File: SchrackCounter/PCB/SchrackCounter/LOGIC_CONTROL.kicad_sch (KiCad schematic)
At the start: 7 parts, among them U2 LDD080BUE-101A, U3 LTD080BUE-103A, U4 LDD080BUE-101A, U5 MAX7219

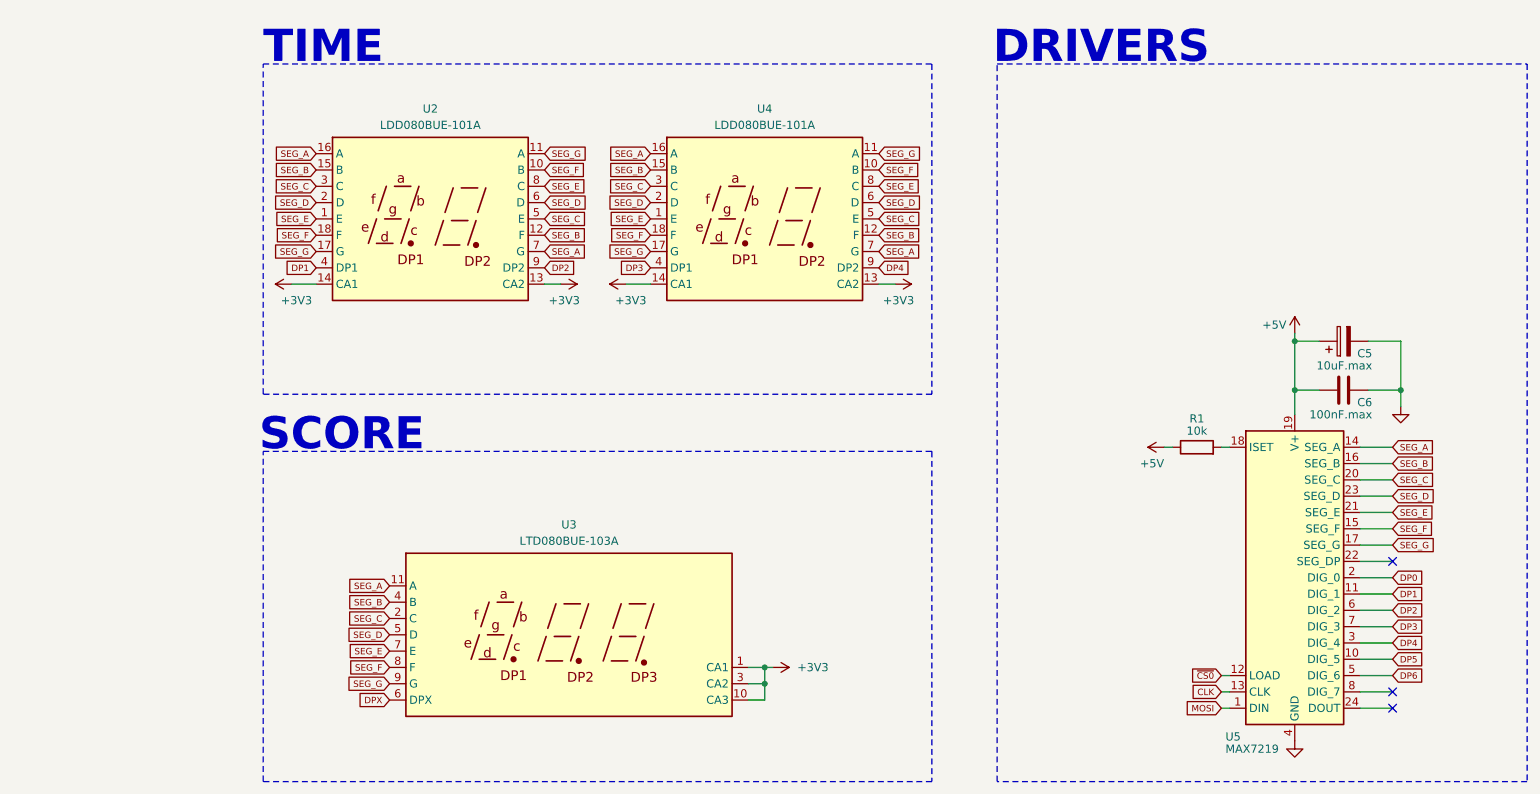
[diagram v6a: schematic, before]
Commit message: PCB update, minor schematic update
PCB routing update, 7segment routing, and minor changes to the 7segments in schematic
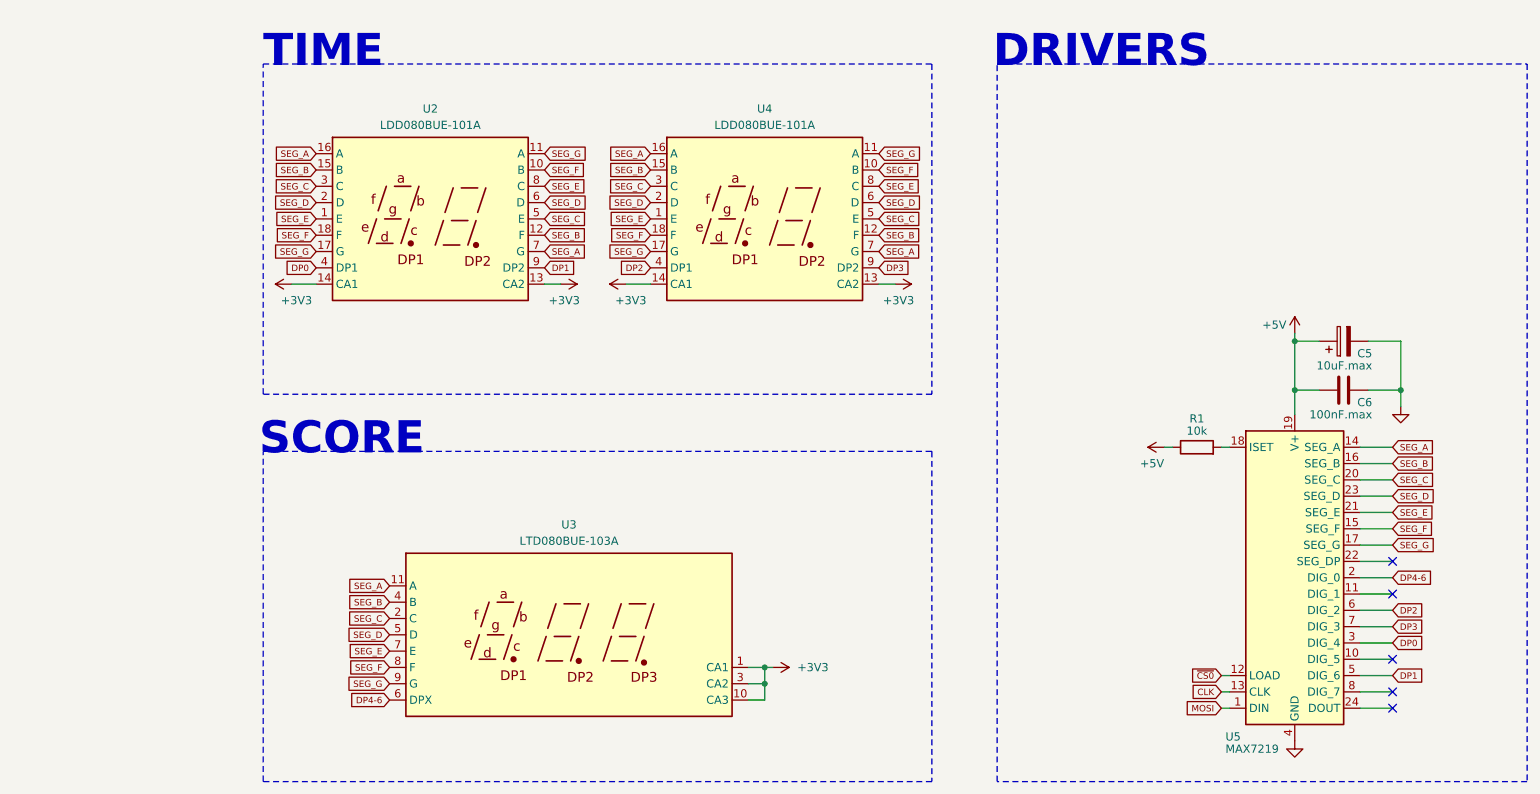
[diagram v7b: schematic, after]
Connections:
- net DP6 is gone; now on net DP1: U5.5 (DIG_6)
- net DP0: now also U2.4 (DP1), U5.3 (DIG_4); no longer U5.2 (DIG_0)
- net DP1: now also U2.9 (DP2); no longer U2.4 (DP1), U5.11 (DIG_1)
- net DP2: now also U4.4 (DP1); no longer U2.9 (DP2)
- net DP3: now also U4.9 (DP2); no longer U4.4 (DP1)
- removed net DP4: U4.9 (DP2), U5.3 (DIG_4)
- net DP5: no longer names the net of U5.10 (DIG_5)
- net DPX renamed DP4-6
- net DP4-6: now also U5.2 (DIG_0)
- no-connect marks 3 -> 5

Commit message: SchrackCounter
PCB Finished
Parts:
- added U8: DC56-11CGKWA, Display_7Segment:DA56-11CGKWA, symbol Display_Character:DC56-11CGKWA
- C5: value 10uF.max -> 10uF
- C6: value 100nF.max -> 100nF
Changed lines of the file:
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@@
 		(dnp no)
 		(fields_autoplaced yes)
-		(property "Reference" "#PWR014"
+		(property "Reference" "#PWR013"
 			(at 223.52 93.98 0)
 			(effects
@@
 			(project "SchrackCounter"
 				(path "/d96f2ffc-3f4c-4f71-b693-29f6b8c3245d/50491303-1200-42ed-9e6c-90c20c198c18"
-					(reference "#PWR014")
+					(reference "#PWR013")
 					(unit 1)
 				)
@@
 	)
 	(symbol
+		(lib_id "Display_Character:DC56-11CGKWA")
+		(at 22.86 73.66 0)
+		(unit 1)
+		(exclude_from_sim no)
+		(in_bom yes)
+		(on_board yes)
+		(dnp no)
+		(fields_autoplaced yes)
+		(property "Reference" "U8"
+			(at 22.86 55.88 0)
+			(effects
+				(font
+					(size 1.27 1.27)
+				)
+			)
+		)
+		(property "Value" "DC56-11CGKWA"
+			(at 22.86 58.42 0)
+			(effects
+				(font
+					(size 1.27 1.27)
+				)
+			)
+		)
+		(property "Footprint" "Display_7Segment:DA56-11CGKWA"
+			(at 23.368 90.17 0)
+			(effects
+				(font
+					(size 1.27 1.27)
+				)
+				(hide yes)
+			)
+		)
+		(property "Datasheet" "http://www.kingbright.com/attachments/file/psearch/000/00/00/DC56-11CGKWA(Ver.7A).pdf"
+			(at 19.812 71.12 0)
+			(effects
+				(font
+					(size 1.27 1.27)
+				)
+				(hide yes)
+			)
+		)
+		(property "Description" "Double digit 7 segment green LED common cathode"
+			(at 22.86 73.66 0)
+			(effects
+				(font
+					(size 1.27 1.27)
+				)
+				(hide yes)
+			)
+		)
+		(pin "3"
+		)
+		(pin "1"
+		)
+		(pin "5"
+		)
+		(pin "6"
+		)
+		(pin "15"
+		)
+		(pin "11"
+		)
+		(pin "2"
+		)
+		(pin "8"
+		)
+		(pin "9"
+		)
+		(pin "13"
+		)
+		(pin "10"
+		)
+		(pin "16"
+		)
+		(pin "18"
+		)
+		(pin "14"
+		)
+		(pin "4"
+		)
+		(pin "7"
+		)
+		(pin "12"
+		)
+		(pin "17"
+		)
+		(instances
+			(project ""
+				(path "/d96f2ffc-3f4c-4f71-b693-29f6b8c3245d/50491303-1200-42ed-9e6c-90c20c198c18"
+					(reference "U8")
+					(unit 1)
+				)
+			)
+		)
+	)
+	(symbol
 		(lib_id "power:+3V3")
 		(at 144.78 68.58 270)
@@
 		(on_board yes)
 		(dnp no)
-		(property "Reference" "#PWR010"
+		(property "Reference" "#PWR09"
 			(at 140.97 68.58 0)
 			(effects
@@
 			(project "SchrackCounter"
 				(path "/d96f2ffc-3f4c-4f71-b693-29f6b8c3245d/50491303-1200-42ed-9e6c-90c20c198c18"
-					(reference "#PWR010")
+					(reference "#PWR09")
 					(unit 1)
 				)
@@
 			)
 		)
-		(property "Value" "10uF.max"
+		(property "Value" "10uF"
 			(at 219.075 81.28 90)
 			(effects
@@
 			)
 		)
-		(property "Value" "100nF.max"
+		(property "Value" "100nF"
 			(at 219.075 88.9 90)
 			(effects
@@
 		(on_board yes)
 		(dnp no)
-		(property "Reference" "#PWR012"
+		(property "Reference" "#PWR011"
 			(at 207.01 80.01 0)
 			(effects
@@
 			(project "SchrackCounter"
 				(path "/d96f2ffc-3f4c-4f71-b693-29f6b8c3245d/50491303-1200-42ed-9e6c-90c20c198c18"
-					(reference "#PWR012")
+					(reference "#PWR011")
 					(unit 1)
 				)
@@
 		(on_board yes)
 		(dnp no)
-		(property "Reference" "#PWR07"
+		(property "Reference" "#PWR06"
 			(at 88.9 68.58 0)
 			(effects
@@
 			(project "SchrackCounter"
 				(path "/d96f2ffc-3f4c-4f71-b693-29f6b8c3245d/50491303-1200-42ed-9e6c-90c20c198c18"
-					(reference "#PWR07")
+					(reference "#PWR06")
 					(unit 1)
 				)
@@
 		(on_board yes)
 		(dnp no)
-		(property "Reference" "#PWR06"
+		(property "Reference" "#PWR05"
 			(at 54.61 68.58 0)
 			(effects
@@
 			(project "SchrackCounter"
 				(path "/d96f2ffc-3f4c-4f71-b693-29f6b8c3245d/50491303-1200-42ed-9e6c-90c20c198c18"
-					(reference "#PWR06")
+					(reference "#PWR05")
 					(unit 1)
 				)
@@
 		(on_board yes)
 		(dnp no)
-		(property "Reference" "#PWR08"
+		(property "Reference" "#PWR07"
 			(at 106.68 68.58 0)
 			(effects
@@
 			(project "SchrackCounter"
 				(path "/d96f2ffc-3f4c-4f71-b693-29f6b8c3245d/50491303-1200-42ed-9e6c-90c20c198c18"
-					(reference "#PWR08")
+					(reference "#PWR07")
 					(unit 1)
 				)
@@
 		(on_board yes)
 		(dnp no)
-		(property "Reference" "#PWR011"
+		(property "Reference" "#PWR010"
 			(at 190.5 93.98 0)
 			(effects
@@
 			(project "SchrackCounter"
 				(path "/d96f2ffc-3f4c-4f71-b693-29f6b8c3245d/50491303-1200-42ed-9e6c-90c20c198c18"
-					(reference "#PWR011")
+					(reference "#PWR010")
 					(unit 1)
 				)
@@
 		(on_board yes)
 		(dnp no)
-		(property "Reference" "#PWR09"
+		(property "Reference" "#PWR08"
 			(at 121.92 128.27 0)
 			(effects
@@
 			(project "SchrackCounter"
 				(path "/d96f2ffc-3f4c-4f71-b693-29f6b8c3245d/50491303-1200-42ed-9e6c-90c20c198c18"
-					(reference "#PWR09")
+					(reference "#PWR08")
 					(unit 1)
 				)
@@
 		(dnp no)
 		(fields_autoplaced yes)
-		(property "Reference" "#PWR013"
+		(property "Reference" "#PWR012"
 			(at 207.01 146.05 0)
 			(effects
@@
 			(project "SchrackCounter"
 				(path "/d96f2ffc-3f4c-4f71-b693-29f6b8c3245d/50491303-1200-42ed-9e6c-90c20c198c18"
-					(reference "#PWR013")
-					(unit 1)
-				)
+					(reference "#PWR012")
+					(unit 1)
+				)
